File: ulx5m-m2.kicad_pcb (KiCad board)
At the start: 6 copper layers, 22 x 60 mm, 234 parts, among them J101 JTAG_EXT, J102 3V3_PSU, J3 Vcore_sel, J4 JTAG, J5 USB_C_Receptacle, SW1 219-2MST, U1 TLV62569DBV, U10 IS42S16320D-6BLI, U3 MPM3833CGRH-Z, U4 GateMate-CCGM1A1, U5 TLV62569DBV, U6 74LVC1G04GM,115, U7 74LVC2G00HK3-7, U8 74LVC2G00HK3-7, U9 AT25QL321-MBUE-T, X2 511FCA100M000BAG, Y1 ASE2-25.000MHZ-L-C-T

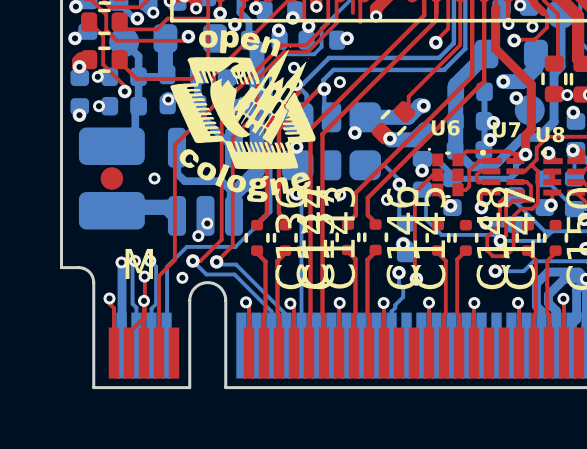
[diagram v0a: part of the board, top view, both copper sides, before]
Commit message: M2 key update - changing resistors back to 1R
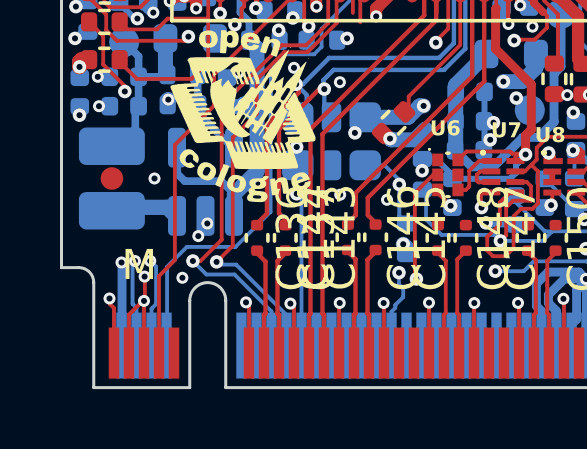
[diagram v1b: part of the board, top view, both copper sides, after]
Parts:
- R105, R106, R23: value 2R -> 1R
